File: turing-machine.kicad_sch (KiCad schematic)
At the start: 120 parts, among them J1 Conn_02x05_Odd_Even, J2 cv, J3 clock, J4 out, J5 noise, J6 Conn_02x08_Odd_Even, J7 Conn_02x08_Odd_Even, Q1 BC547, SW1 SW_Rotary12, SW2 SW_SPDT_MSM, U1 TL074, U10 4050, U11 L78L09_SOT89, U12 4081, U13 4081, U2 DAC08, U3 TL431DBZ, U4 4016, U5 TL072, U6 4015, U7 4015, U8 L78L09_SOT89, U9 4050

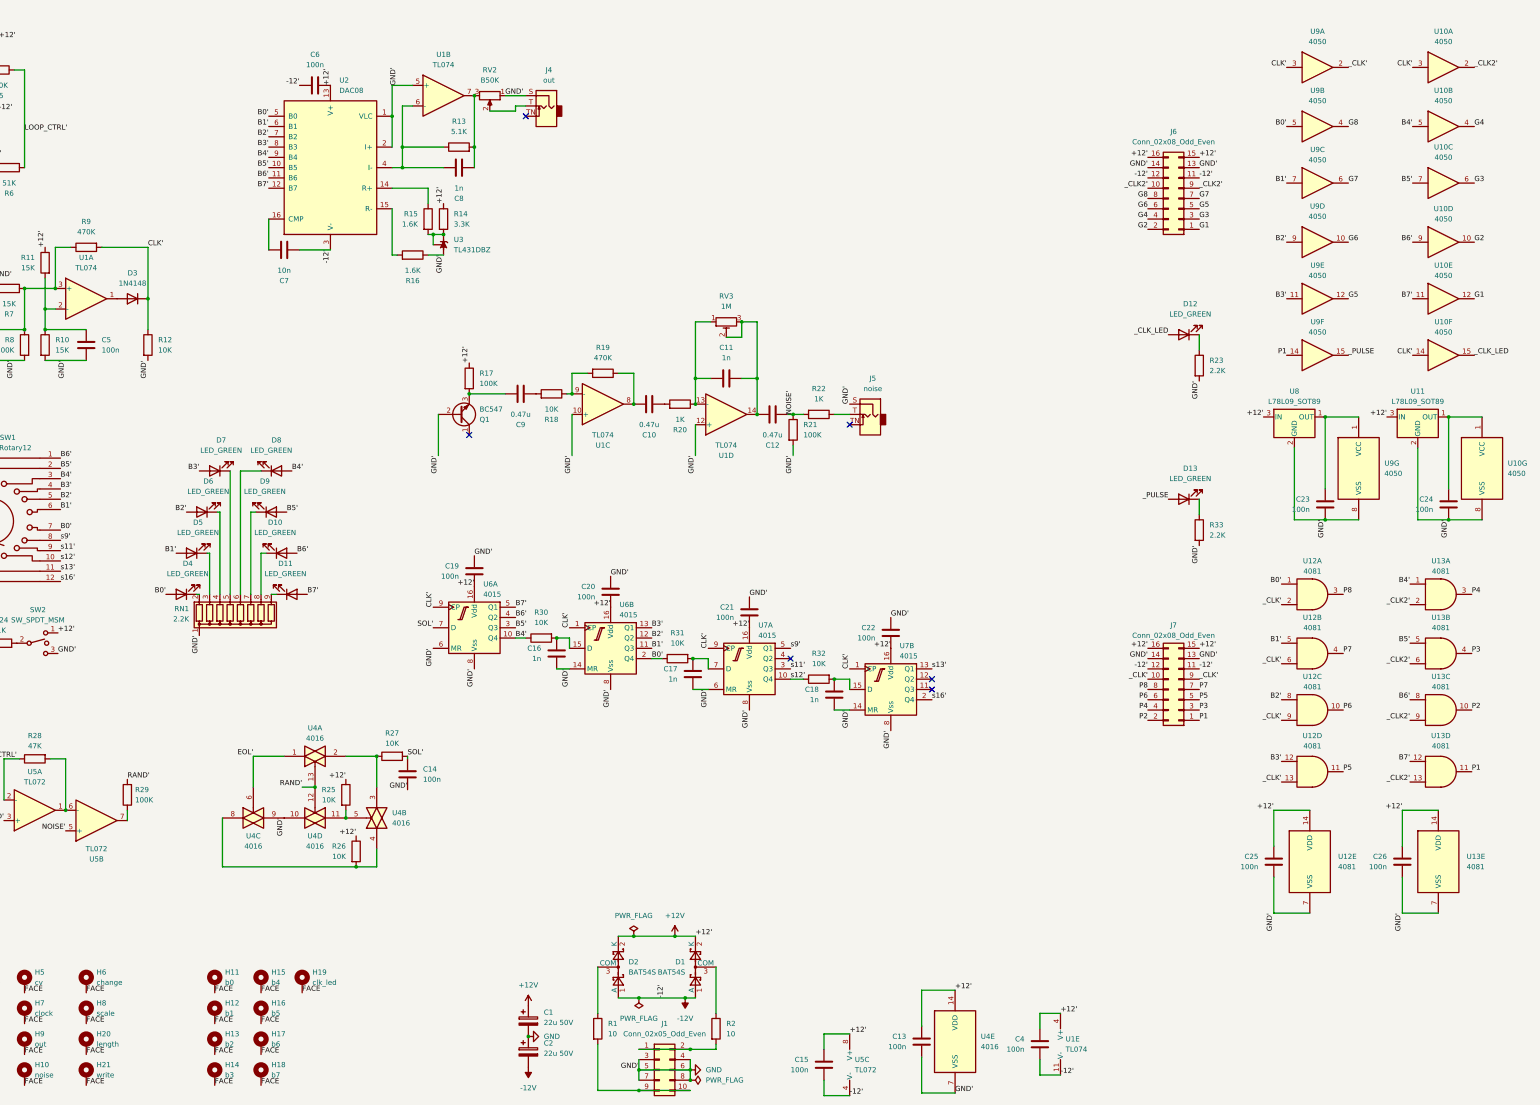
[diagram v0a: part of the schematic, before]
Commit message: PCB layout complete
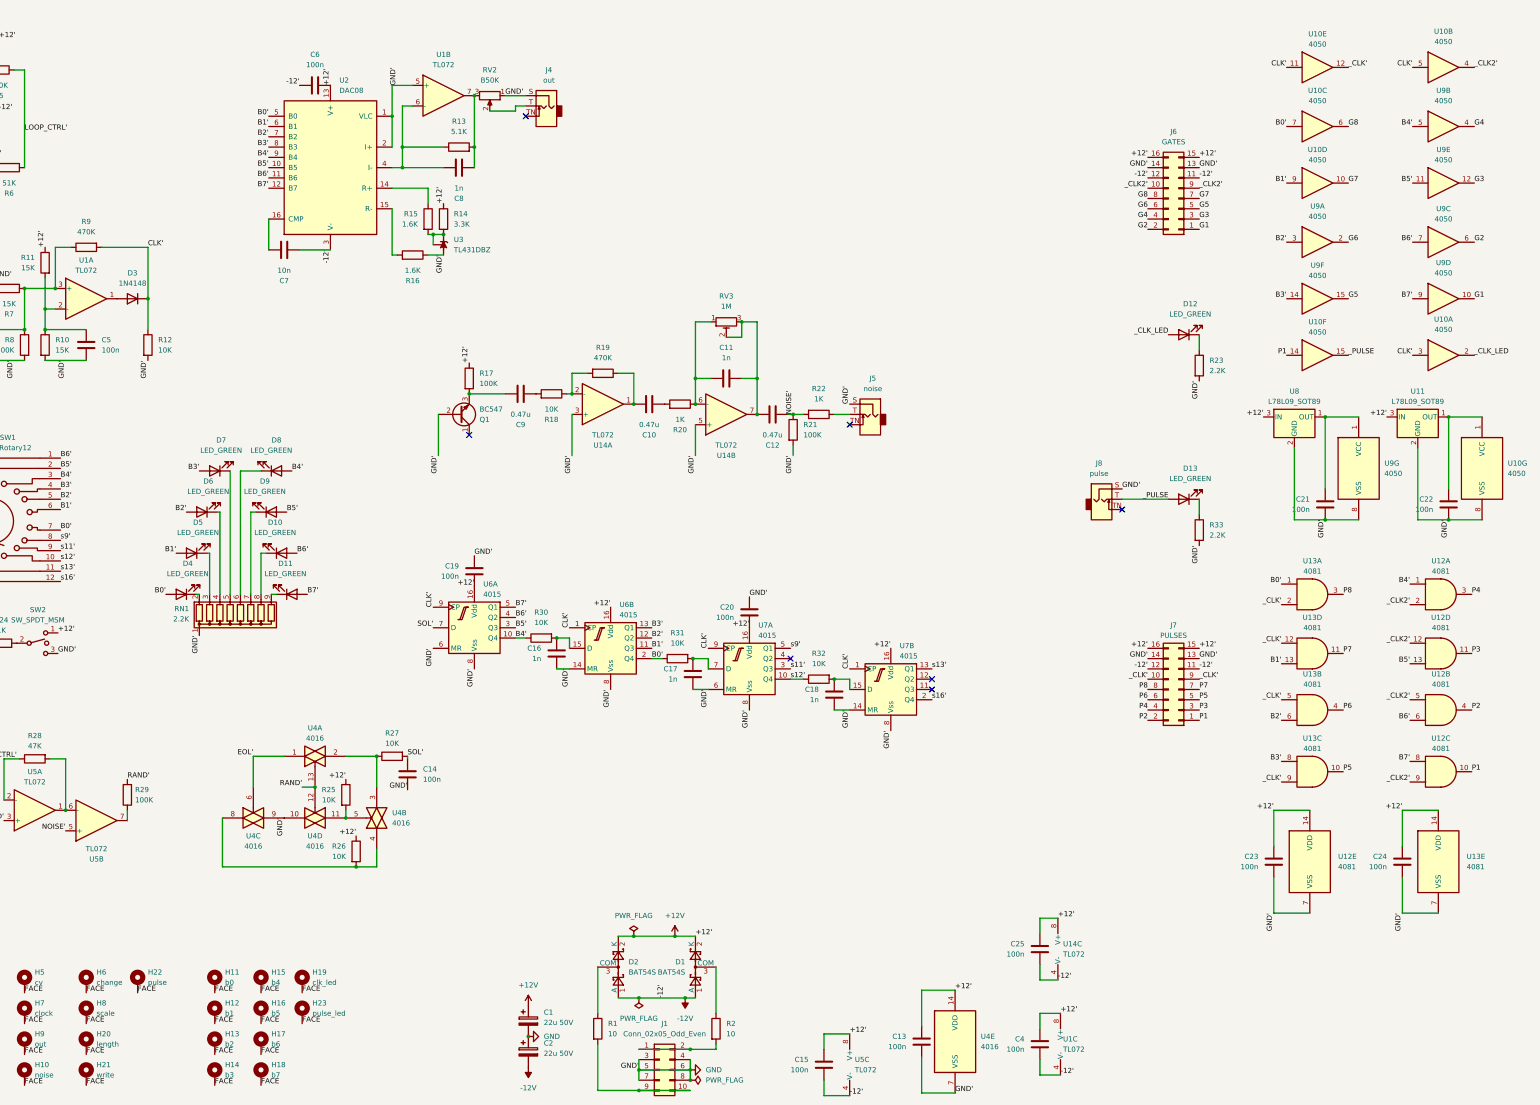
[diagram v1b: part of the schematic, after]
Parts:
- removed C21, C22: 100n, Capacitor_SMD:C_0805_2012Metric, symbol Device:C
- removed U1: TL074, Package_SO:SOIC-14_3.9x8.7mm_P1.27mm, symbol Amplifier_Operational:TL074
- added C25: 100n, Capacitor_SMD:C_0805_2012Metric, symbol Device:C
- added H22: pulse, Eurorack:Mech-AudioJack-Hole-Output-Gate, symbol Mechanical:MountingHole_Pad
- added H23: pulse_led, Eurorack:Mech-LED-Hole-3mm, symbol Mechanical:MountingHole_Pad
- added J8: pulse, Eurorack:AudioJack2_Tayda_A-2566, symbol Eurorack:AudioJack2_SwitchT
- added U1, U14: TL072, Package_SO:SOIC-8_3.9x4.9mm_P1.27mm, symbol Amplifier_Operational:TL072
- H10: footprint Eurorack:Mech-MountingHole -> Eurorack:Mech-AudioJack-Hole-Output
- H11, H12, H13, H14, H15, H16, H17, H18, H19: footprint Eurorack:Mech-MountingHole -> Eurorack:Mech-LED-Hole-3mm
- H20: footprint Eurorack:Mech-MountingHole -> Eurorack:Mech-MRK-Hole
- H21: footprint Eurorack:Mech-MountingHole -> Eurorack:Mech-2M_Switch-Hole
- H5: footprint Eurorack:Mech-MountingHole -> Eurorack:Mech-AudioJack-Hole-Input-CV
- H6: footprint Eurorack:Mech-MountingHole -> Eurorack:Mech-Potentiometer-Hole_level_180deg
- H7: footprint Eurorack:Mech-MountingHole -> Eurorack:Mech-AudioJack-Hole-Input-Clock
- H8: footprint Eurorack:Mech-MountingHole -> Eurorack:Mech-Potentiometer-Hole_level
- H9: footprint Eurorack:Mech-MountingHole -> Eurorack:Mech-AudioJack-Hole-Output-CV
- J6: value Conn_02x08_Odd_Even -> GATES
- J7: value Conn_02x08_Odd_Even -> PULSES
- SW2: footprint Capacitor_THT:C_Rect_L7.2mm_W2.5mm_P5.00mm_FKS2_FKP2_MKS2_MKP2 -> Eurorack:Switch_SPDT_Tayda_A-5751
- renumbered C23 to C21, C24 to C22, C25 to C23, C26 to C24
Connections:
- net +12V: now also C25.1, U1.8 (V+), U14.8 (V+)
- net -12V: now also C25.2, U1.4 (V-), U14.4 (V-)
- net B0': now also U10.7, U13.1; no longer U12.1, U9.5
- net B1': now also U10.9, U13.13; no longer U12.5, U9.7
- net B2': now also U13.6, U9.3; no longer U12.8, U9.9
- net B3': now also U13.8, U9.14; no longer U12.12, U9.11
- net B4': now also U12.1, U9.5; no longer U10.5, U13.1
- net B5': now also U12.13, U9.11; no longer U10.7, U13.5
- net B6': now also U12.6, U9.7; no longer U10.9, U13.8
- net B7': now also U12.8, U9.9; no longer U10.11, U13.12
- net CLK': now also U10.11, U10.5; no longer U10.14, U9.3
- net FACE: now also H22.1, H23.1
- net G1: now also U9.10; no longer U10.12
- net G2: now also U9.6; no longer U10.10
- net G3: now also U9.12; no longer U10.6
- net G4: now also U9.4; no longer U10.4
- net G5: now also U9.15; no longer U9.12
- net G6: now also U9.2; no longer U9.10
- net G7: now also U10.10; no longer U9.6
- net G8: now also U10.6; no longer U9.4
- net GND: now also J8.S, U1.5 (+), U14.3 (+), U14.5 (+)
- net P1: now also U10.14, U12.10; no longer U13.11, U9.14
- net P2: now also U12.4; no longer U13.10
- net P3: now also U12.11; no longer U13.4
- net P4: now also U12.3; no longer U13.3
- net P5: now also U13.10; no longer U12.11
- net P6: now also U13.4; no longer U12.10
- net P7: now also U13.11; no longer U12.4
- net P8: now also U13.3; no longer U12.3
- net _CLK': now also U10.12, U13.12, U13.2, U13.5, U13.9; no longer U12.13, U12.2, U12.6, U12.9, U9.2
- net _CLK2': now also U10.4, U12.12, U12.2, U12.5, U12.9; no longer U10.2, U13.13, U13.2, U13.6, U13.9
- net _CLK_LED: now also U10.2; no longer U10.15
- net _PULSE: now also U10.15, J8.T; no longer U9.15
- net at C10.1, R19.1: now also U14.1
- net at R18.1, R19.2: now also U14.2 (-)
- net at C11.2, C12.1, RV3.2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: now also U14.7
- net at C11.1, R20.1, RV3.1: now also U14.6 (-)
- net at C5.1, R10.1, R11.2: now also U1.2 (-)
- net at C8.1, R13.1, U2.4 (I-): now also U1.6 (-)
- net at C8.2, R13.2, RV2.3: now also U1.7
- net at C3.1, R7.1, R8.1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: now also U1.3 (+)
- net at D3.2 (A): now also U1.1
- no-connect marks 8 -> 9
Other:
- moved on the sheet: C20, U10A, U10B, U10C, U10D, U10E, U10F, U12A, U12B, U12C, U12D, U13A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

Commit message: fix: getting all parts sorted out
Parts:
- removed J6: GATES, Eurorack:PinHeader_2x08_P2.54mm_Vertical, symbol Connector_Generic:Conn_02x08_Odd_Even
- removed J7: PULSES, Eurorack:PinHeader_2x08_P2.54mm_Vertical, symbol Connector_Generic:Conn_02x08_Odd_Even
- added J6, J7: Conn_02x08_Odd_Even, Eurorack:PinHeader_2x08_P2.54mm_Vertical, symbol Eurorack:Conn_02x08_Odd_Even
- C10, C12, C9: value 0.47u -> 470n box
- SW1: PartNum (none) -> 633-MRK112-BA; Vendor (none) -> Mouser
- SW2: footprint Eurorack:Switch_SPDT_Tayda_A-5751 -> Eurorack:Switch_SPDT_1M_Solder_Lug; PartNum (none) -> A-6099; Vendor (none) -> Tayda
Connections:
- net +12V: now also J6.15 (Pin_15), J6.16 (Pin_16), J7.15 (Pin_15), J7.16 (Pin_16)
- net -12V: now also J6.11 (Pin_11), J6.12 (Pin_12), J7.11 (Pin_11), J7.12 (Pin_12)
- net G1: now also J6.1 (Pin_1)
- net G2: now also J6.2 (Pin_2)
- net G3: now also J6.3 (Pin_3)
- net G4: now also J6.4 (Pin_4)
- net G5: now also J6.5 (Pin_5)
- net G6: now also J6.6 (Pin_6)
- net G7: now also J6.7 (Pin_7)
- net G8: now also J6.8 (Pin_8)
- net GND: now also J6.13 (Pin_13), J6.14 (Pin_14), J7.13 (Pin_13), J7.14 (Pin_14)
- net P1: now also J7.1 (Pin_1)
- net P2: now also J7.2 (Pin_2)
- net P3: now also J7.3 (Pin_3)
- net P4: now also J7.4 (Pin_4)
- net P5: now also J7.5 (Pin_5)
- net P6: now also J7.6 (Pin_6)
- net P7: now also J7.7 (Pin_7)
- net P8: now also J7.8 (Pin_8)
- net _CLK': now also J7.10 (Pin_10), J7.9 (Pin_9)
- net _CLK2': now also J6.10 (Pin_10), J6.9 (Pin_9)
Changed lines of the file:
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@@
       (effects (font (size 1.27 1.27)))
     )
-    (property "Value" "0.47u" (at 158.115 114.3 90)
+    (property "Value" "470n box" (at 158.115 114.3 90)
       (effects (font (size 1.27 1.27)))
     )
@@
       (effects (font (size 1.27 1.27)))
     )
-    (property "Value" "0.47u" (at 220.345 119.38 90)
+    (property "Value" "470n box" (at 220.345 119.38 90)
       (effects (font (size 1.27 1.27)))
     )
@@
       (effects (font (size 1.27 1.27)))
     )
-    (property "Footprint" "Eurorack:Switch_SPDT_Tayda_A-5751" (at 38.735 170.815 0)
+    (property "Footprint" "Eurorack:Switch_SPDT_1M_Solder_Lug" (at 38.735 170.815 0)
       (effects (font (size 1.27 1.27)) hide)
     )
@@
       (effects (font (size 1.27 1.27)) hide)
     )
+    (property "Vendor" "Tayda" (at 38.735 170.815 0)
+      (effects (font (size 1.27 1.27)) hide)
+    )
+    (property "PartNum" "A-6099" (at 38.735 170.815 0)
+      (effects (font (size 1.27 1.27)) hide)
+    )
     (pin "2")
     (pin "1")
@@
     )
   )
+  (symbol (lib_id "Eurorack:Conn_02x08_Odd_Even") (at 320.675 60.96 180) (unit 1)
+    (in_bom yes) (on_board yes) (dnp no) (fields_autoplaced)
+    (property "Reference" "J6" (at 319.405 44.45 0)
+      (effects (font (size 1.27 1.27)))
+    )
+    (property "Value" "Conn_02x08_Odd_Even" (at 319.405 46.99 0)
+      (effects (font (size 1.27 1.27)))
+    )
+    (property "Footprint" "Eurorack:PinHeader_2x08_P2.54mm_Vertical" (at 320.675 60.96 0)
+      (effects (font (size 1.27 1.27)) hide)
+    )
+    (property "Datasheet" "~" (at 320.675 60.96 0)
+      (effects (font (size 1.27 1.27)) hide)
+    )
+    (property "Vendor" "Tayda" (at 320.675 60.96 0)
+      (effects (font (size 1.27 1.27)) hide)
+    )
+    (property "PartNum" "A-2956" (at 320.675 60.96 0)
+      (effects (font (size 1.27 1.27)) hide)
+    )
+    (pin "16")
+    (pin "15")
+    (pin "2")
+    (pin "7")
+    (pin "9")
+    (pin "1")
+    (pin "14")
+    (pin "10")
+    (pin "13")
+    (pin "8")
+    (pin "4")
+    (pin "3")
+    (pin "5")
+    (pin "6")
+    (pin "11")
+    (pin "12")
+    (instances
+      (project "turing-machine"
+        (path "/54607e40-577c-4def-b17c-96859aef0795"
+          (reference "J6") (unit 1)
+        )
+      )
+    )
+  )
   (symbol (lib_id "Device:R_Potentiometer_Trim") (at 208.915 91.44 90) (mirror x) (unit 1)
     (in_bom yes) (on_board yes) (dnp no)
@@
     )
   )
-  (symbol (lib_id "Connector_Generic:Conn_02x08_Odd_Even") (at 320.675 60.96 180) (unit 1)
-    (in_bom yes) (on_board yes) (dnp no) (fields_autoplaced)
-    (property "Reference" "J6" (at 319.405 44.45 0)
-      (effects (font (size 1.27 1.27)))
-    )
-    (property "Value" "GATES" (at 319.405 46.99 0)
-      (effects (font (size 1.27 1.27)))
-    )
-    (property "Footprint" "Eurorack:PinHeader_2x08_P2.54mm_Vertical" (at 320.675 60.96 0)
-      (effects (font (size 1.27 1.27)) hide)
-    )
-    (property "Datasheet" "~" (at 320.675 60.96 0)
-      (effects (font (size 1.27 1.27)) hide)
-    )
-    (pin "6")
-    (pin "8")
-    (pin "7")
-    (pin "4")
-    (pin "3")
-    (pin "9")
-    (pin "5")
-    (pin "11")
-    (pin "2")
-    (pin "1")
-    (pin "15")
-    (pin "12")
-    (pin "16")
-    (pin "14")
-    (pin "13")
-    (pin "10")
-    (instances
-      (project "turing-machine"
-        (path "/54607e40-577c-4def-b17c-96859aef0795"
-          (reference "J6") (unit 1)
-        )
-      )
-    )
-  )
   (symbol (lib_id "Amplifier_Operational:TL072") (at 50.8 85.725 0) (unit 1)
     (in_bom yes) (on_board yes) (dnp no) (fields_autoplaced)
@@
     )
   )
+  (symbol (lib_id "Eurorack:Conn_02x08_Odd_Even") (at 320.675 182.245 180) (unit 1)
+    (in_bom yes) (on_board yes) (dnp no) (fields_autoplaced)
+    (property "Reference" "J7" (at 319.405 166.37 0)
+      (effects (font (size 1.27 1.27)))
+    )
+    (property "Value" "Conn_02x08_Odd_Even" (at 319.405 168.91 0)
+      (effects (font (size 1.27 1.27)))
+    )
+    (property "Footprint" "Eurorack:PinHeader_2x08_P2.54mm_Vertical" (at 320.675 182.245 0)
+      (effects (font (size 1.27 1.27)) hide)
+    )
+    (property "Datasheet" "~" (at 320.675 182.245 0)
+      (effects (font (size 1.27 1.27)) hide)
+    )
+    (property "Vendor" "Tayda" (at 320.675 182.245 0)
+      (effects (font (size 1.27 1.27)) hide)
+    )
+    (property "PartNum" "A-2956" (at 320.675 182.245 0)
+      (effects (font (size 1.27 1.27)) hide)
+    )
+    (pin "5")
+    (pin "4")
+    (pin "7")
+    (pin "14")
+    (pin "8")
+    (pin "3")
+    (pin "1")
+    (pin "11")
+    (pin "15")
+    (pin "13")
+    (pin "9")
+    (pin "16")
+    (pin "2")
+    (pin "6")
+    (pin "10")
+    (pin "12")
+    (instances
+      (project "turing-machine"
+        (path "/54607e40-577c-4def-b17c-96859aef0795"
+          (reference "J7") (unit 1)
+        )
+      )
+    )
+  )
   (symbol (lib_id "4xxx:4050") (at 354.965 99.695 0) (unit 6)
     (in_bom yes) (on_board yes) (dnp no) (fields_autoplaced)
@@
     )
   )
-  (symbol (lib_id "Connector_Generic:Conn_02x08_Odd_Even") (at 320.675 182.245 180) (unit 1)
-    (in_bom yes) (on_board yes) (dnp no) (fields_autoplaced)
-    (property "Reference" "J7" (at 319.405 166.37 0)
-      (effects (font (size 1.27 1.27)))
-    )
-    (property "Value" "PULSES" (at 319.405 168.91 0)
-      (effects (font (size 1.27 1.27)))
-    )
-    (property "Footprint" "Eurorack:PinHeader_2x08_P2.54mm_Vertical" (at 320.675 182.245 0)
-      (effects (font (size 1.27 1.27)) hide)
-    )
-    (property "Datasheet" "~" (at 320.675 182.245 0)
-      (effects (font (size 1.27 1.27)) hide)
-    )
-    (pin "6")
-    (pin "8")
-    (pin "7")
-    (pin "4")
-    (pin "3")
-    (pin "9")
-    (pin "5")
-    (pin "11")
-    (pin "2")
-    (pin "1")
-    (pin "15")
-    (pin "12")
-    (pin "16")
-    (pin "14")
-    (pin "13")
-    (pin "10")
-    (instances
-      (project "turing-machine"
-        (path "/54607e40-577c-4def-b17c-96859aef0795"
-          (reference "J7") (unit 1)
-        )
-      )
-    )
-  )
   (symbol (lib_id "Device:R") (at 126.365 198.755 90) (mirror x) (unit 1)
     (in_bom yes) (on_board yes) (dnp no) (fields_autoplaced)
@@
       (effects (font (size 1.27 1.27)) hide)
     )
+    (property "Vendor" "Mouser" (at 34.29 140.335 0)
+      (effects (font (size 1.27 1.27)) hide)
+    )
+    (property "PartNum" "633-MRK112-BA" (at 34.29 140.335 0)
+      (effects (font (size 1.27 1.27)) hide)
+    )
     (pin "13")
     (pin "9")
@@
       (effects (font (size 1.27 1.27)))
     )
-    (property "Value" "0.47u" (at 189.865 116.84 90)
+    (property "Value" "470n box" (at 189.865 116.84 90)
       (effects (font (size 1.27 1.27)))
     )

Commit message: fix: available parts only
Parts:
- C10, C12, C9: footprint Capacitor_THT:C_Rect_L7.2mm_W2.5mm_P5.00mm_FKS2_FKP2_MKS2_MKP2 -> Capacitor_THT:C_Rect_L7.2mm_W4.5mm_P5.00mm_FKS2_FKP2_MKS2_MKP2
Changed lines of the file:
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@@
       (effects (font (size 1.27 1.27)))
     )
-    (property "Footprint" "Capacitor_THT:C_Rect_L7.2mm_W2.5mm_P5.00mm_FKS2_FKP2_MKS2_MKP2" (at 161.925 110.1852 0)
+    (property "Footprint" "Capacitor_THT:C_Rect_L7.2mm_W4.5mm_P5.00mm_FKS2_FKP2_MKS2_MKP2" (at 161.925 110.1852 0)
       (effects (font (size 1.27 1.27)) hide)
     )
@@
       (effects (font (size 1.27 1.27)))
     )
-    (property "Footprint" "Capacitor_THT:C_Rect_L7.2mm_W2.5mm_P5.00mm_FKS2_FKP2_MKS2_MKP2" (at 224.155 115.2652 0)
+    (property "Footprint" "Capacitor_THT:C_Rect_L7.2mm_W4.5mm_P5.00mm_FKS2_FKP2_MKS2_MKP2" (at 224.155 115.2652 0)
       (effects (font (size 1.27 1.27)) hide)
     )
@@
       (effects (font (size 1.27 1.27)))
     )
-    (property "Footprint" "Capacitor_THT:C_Rect_L7.2mm_W2.5mm_P5.00mm_FKS2_FKP2_MKS2_MKP2" (at 193.675 112.7252 0)
+    (property "Footprint" "Capacitor_THT:C_Rect_L7.2mm_W4.5mm_P5.00mm_FKS2_FKP2_MKS2_MKP2" (at 193.675 112.7252 0)
       (effects (font (size 1.27 1.27)) hide)
     )
